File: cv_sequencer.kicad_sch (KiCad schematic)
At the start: 65 parts, among them J1 :MIDI_IO, J2 4005_SWD_Header, J3 3086_Connector_Eurorack_Power, J4 3096_USBC_RA_SMD, SW1 RST, SW2 BOOT, U1 3097_TFT_Display_SPI, U10 PWR, U11 STAT, U12 4048_W25Q16JVSSIQ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

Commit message: Updated a few things from testing voltage regulators
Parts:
- TP10: value 5V3 -> 5V1
- TP9: value 3V1 -> 3V0
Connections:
- net 5V3 renamed 5V1
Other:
- sheet IO Jacks ports: added IO_5V1; removed IO_5V3
- note added: "Measured = 2.96V"
- note added: "Measured = 5.16V"
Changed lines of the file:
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@@
     (effects (font (size 1.27 1.27) (thickness 0.254) bold) (justify left bottom))
+  )
+  (text "Measured = 5.16V" (at 171.45 79.375 0)
+    (effects (font (size 1.27 1.27) (thickness 0.254) bold italic) (justify left bottom))
   )
   (text "GPIO13:14 Function 5 (SIO)" (at 38.735 151.765 0)
@@
     (effects (font (size 1.27 1.27)) (justify left bottom))
   )
-  (label "5V3" (at 163.83 114.935 0)
+  (label "5V1" (at 163.83 114.935 0)
     (effects (font (size 1.27 1.27)) (justify left bottom))
   )
@@
     (effects (font (size 1.27 1.27)) (justify left bottom))
   )
-  (label "5V3" (at 153.67 55.88 0)
+  (label "5V1" (at 153.67 55.88 0)
     (effects (font (size 1.27 1.27)) (justify left bottom))
   )
@@
     (effects (font (size 1.27 1.27)) (justify right bottom))
   )
-  (label "5V3" (at 63.5 25.4 180)
+  (label "5V1" (at 63.5 25.4 180)
     (effects (font (size 1.27 1.27)) (justify right bottom))
   )
@@
   )
   (symbol (lib_id "Shulltronics_Passives:4021_Resistor_SMD_Jumper") (at 69.85 31.75 0) (unit 1)
-    (in_bom yes) (on_board yes) (fields_autoplaced)
+    (in_bom yes) (on_board yes)
     (property "Reference" "R3" (id 0) (at 72.39 30.4799 0)
       (effects (font (size 1.27 1.27)) (justify left))
@@
       (effects (font (size 1.27 1.27)) (justify left))
     )
-    (property "Value" "3V1" (id 1) (at 135.89 26.67 0)
+    (property "Value" "3V0" (id 1) (at 135.89 26.67 0)
       (effects (font (size 1.27 1.27)) (justify left))
     )
@@
       (effects (font (size 1.27 1.27)) (justify left))
     )
-    (property "Value" "5V3" (id 1) (at 148.59 57.15 90)
+    (property "Value" "5V1" (id 1) (at 148.59 57.15 90)
       (effects (font (size 1.27 1.27)) (justify left))
     )
@@
       (effects (font (size 1.27 1.27)) (justify left))
     )
-    (pin "IO_5V3" input (at 172.72 121.285 180)
+    (pin "IO_5V1" input (at 172.72 121.285 180)
       (effects (font (size 1.27 1.27)) (justify left))
     )
@@
       (reference "C24") (unit 1) (value "3089_Capacitor_100n_16V_SMD") (footprint "Shulltronics_Generics:C_0402_HandSolder")
     )
+    (path "/4dfe3baa-4352-450f-8be2-7b95dd9dc153/59fc35d7-90b3-4b2b-a74b-b1e13b31b067"
+      (reference "C25") (unit 1) (value "4013_Capacitor_1u_16V_0402") (footprint "Shulltronics_Generics:C_0402_HandSolder")
+    )
+    (path "/4dfe3baa-4352-450f-8be2-7b95dd9dc153/ecbebc57-6cc8-4996-919b-3bb0a8acac97"
+      (reference "C26") (unit 1) (value "4035_Capacitor_2u2_25V_0402") (footprint "Shulltronics_Generics:C_0402_HandSolder")
+    )
     (path "/16a49ecd-abfd-4d6b-abb3-2f90d5cb3b16"
       (reference "E1") (unit 1) (value "4025_Encoder_Switch_SMD") (footprint "Shulltronics_ElectroMechanical:4025_Encoder_PEC11S")
@@
     )
     (path "/f37d5281-d51b-448e-b4fa-666b2af6d522"
-      (reference "TP9") (unit 1) (value "3V1") (footprint "Shulltronics_Generics:TestPoint_Pad_D2.0mm")
+      (reference "TP9") (unit 1) (value "3V0") (footprint "Shulltronics_Generics:TestPoint_Pad_D2.0mm")
     )
     (path "/f7efade5-ccc5-4eec-8b83-7648f2629c59"
-      (reference "TP10") (unit 1) (value "5V3") (footprint "Shulltronics_Generics:TestPoint_Pad_D2.0mm")
+      (reference "TP10") (unit 1) (value "5V1") (footprint "Shulltronics_Generics:TestPoint_Pad_D2.0mm")
     )
     (path "/3b0f9e31-fd5d-41bd-a834-81a48691dd1c"

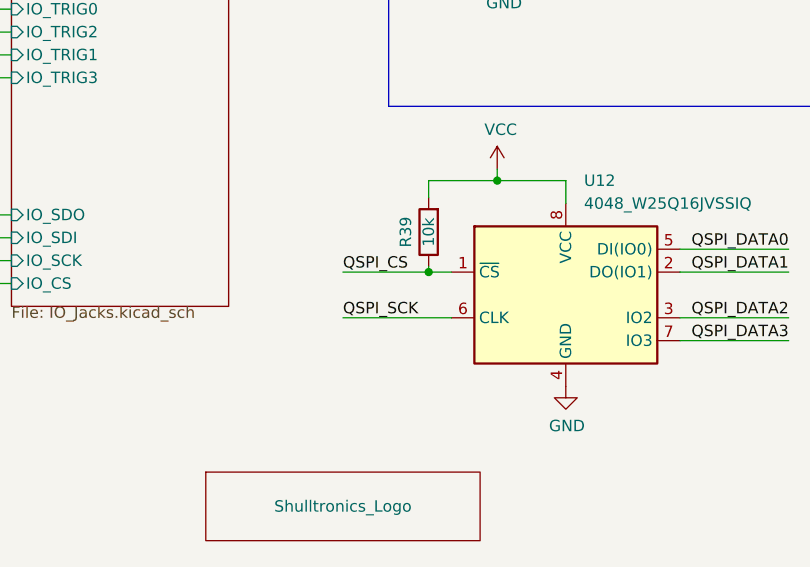
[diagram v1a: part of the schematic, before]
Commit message: Added components and routed for 5v0 reference
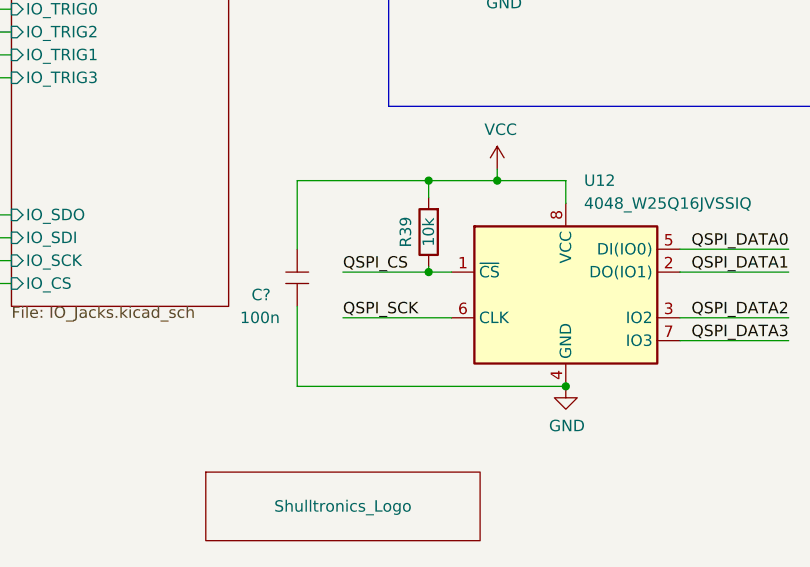
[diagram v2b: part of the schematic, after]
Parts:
- added C?: 3089_Capacitor_100n_16V_0402, Shulltronics_Generics:C_0402_HandSolder, symbol Shulltronics_Passives:3089_Capacitor_100n_16V_0402
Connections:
- net GND: now also C?.1
- net VCC: now also C?.2
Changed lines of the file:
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@@
     (pin "1")
+  )
+  (symbol (lib_id "Shulltronics_Passives:3089_Capacitor_100n_16V_0402") (at 204.47 153.035 90) (unit 1)
+    (in_bom yes) (on_board yes)
+    (property "Reference" "C?" (id 0) (at 199.39 155.575 90)
+      (effects (font (size 1.27 1.27)) (justify right))
+    )
+    (property "Value" "3089_Capacitor_100n_16V_0402" (id 1) (at 212.09 153.035 0)
+      (effects (font (size 1.27 1.27)) hide)
+    )
+    (property "Footprint" "Shulltronics_Generics:C_0402_HandSolder" (id 2) (at 209.55 153.035 0)
+      (effects (font (size 1.27 1.27)) hide)
+    )
+    (property "Datasheet" "https://media.digikey.com/pdf/Data%20Sheets/Samsung%20PDFs/CL05A104KA5NNNC.pdf" (id 3) (at 214.63 153.035 0)
+      (effects (font (size 1.27 1.27)) hide)
+    )
+    (property "SPN" "3089" (id 4) (at 207.01 153.035 0)
+      (effects (font (size 1.27 1.27)) hide)
+    )
+    (property "Val" "100n" (id 5) (at 198.12 158.115 90)
+      (effects (font (size 1.27 1.27)) (justify right))
+    )
+    (pin "1")
+    (pin "2")
   )
   (symbol (lib_id "Shulltronics_DevBoards:3097_TFT_Display_SPI") (at 95.25 29.21 0) (unit 1)
@@
       (reference "C26") (unit 1) (value "4035_Capacitor_2u2_25V_0402") (footprint "Shulltronics_Generics:C_0402_HandSolder")
     )
+    (path "/72b9c7ac-e6a3-4bb6-8bb5-60b67975d365"
+      (reference "C?") (unit 1) (value "3089_Capacitor_100n_16V_0402") (footprint "Shulltronics_Generics:C_0402_HandSolder")
+    )
     (path "/16a49ecd-abfd-4d6b-abb3-2f90d5cb3b16"
